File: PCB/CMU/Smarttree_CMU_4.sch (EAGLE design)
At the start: 43 parts, among them X2 057-006-0

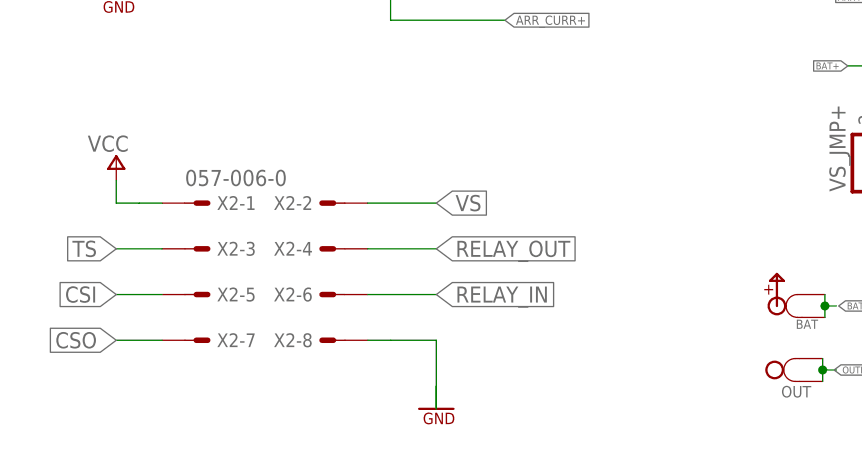
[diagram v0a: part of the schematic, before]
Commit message: new connector on cmu
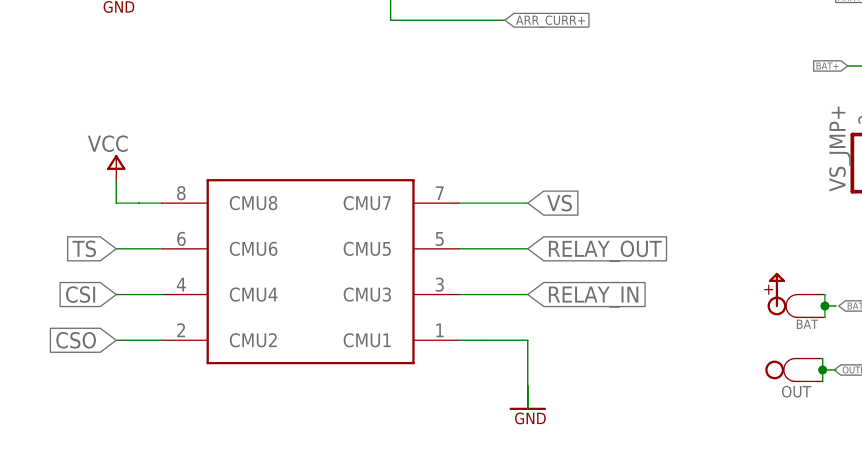
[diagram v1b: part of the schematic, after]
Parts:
- removed X2: 057-006-0, con-panduit:057-006-0
- added U$1: 8PINCONN, SmartTreeCan:8PINCONN
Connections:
- net CSI: now also U$1.CMU4; no longer X2-5.S
- net CSO: now also U$1.CMU2; no longer X2-7.S
- net GND: now also U$1.CMU1; no longer X2-8.S
- net RELAY_IN: now also U$1.CMU3; no longer X2-6.S
- net RELAY_OUT: now also U$1.CMU5; no longer X2-4.S
- net TS: now also U$1.CMU6; no longer X2-3.S
- net VCC: now also U$1.CMU8; no longer X2-1.S
- net VS: now also U$1.CMU7; no longer X2-2.S
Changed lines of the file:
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@@
 <layer number="54" name="bGND_GNDA" color="1" fill="9" visible="no" active="no"/>
 <layer number="56" name="wert" color="7" fill="1" visible="no" active="no"/>
+<layer number="57" name="tCAD" color="7" fill="1" visible="no" active="no"/>
+<layer number="59" name="tCarbon" color="7" fill="1" visible="no" active="no"/>
+<layer number="60" name="bCarbon" color="7" fill="1" visible="no" active="no"/>
 <layer number="90" name="Modules" color="5" fill="1" visible="yes" active="yes"/>
 <layer number="91" name="Nets" color="2" fill="1" visible="yes" active="yes"/>
@@
 <layer number="97" name="Info" color="7" fill="1" visible="no" active="yes"/>
 <layer number="98" name="Guide" color="6" fill="1" visible="no" active="yes"/>
+<layer number="99" name="SpiceOrder" color="7" fill="1" visible="yes" active="yes"/>
 <layer number="100" name="Muster" color="7" fill="1" visible="no" active="no"/>
 <layer number="101" name="Patch_Top" color="12" fill="4" visible="no" active="yes"/>
@@
 <layer number="111" name="LPC17xx" color="7" fill="1" visible="no" active="yes"/>
 <layer number="112" name="tSilk" color="7" fill="1" visible="no" active="yes"/>
+<layer number="113" name="IDFDebug" color="4" fill="1" visible="yes" active="yes"/>
 <layer number="116" name="Patch_BOT" color="9" fill="4" visible="no" active="yes"/>
+<layer number="118" name="Rect_Pads" color="7" fill="1" visible="yes" active="yes"/>
 <layer number="121" name="_tsilk" color="7" fill="1" visible="no" active="yes"/>
 <layer number="122" name="_bsilk" color="7" fill="1" visible="no" active="yes"/>
@@
 <layer number="127" name="_tValues" color="7" fill="1" visible="no" active="yes"/>
 <layer number="128" name="_bValues" color="7" fill="1" visible="no" active="yes"/>
+<layer number="129" name="Mask" color="7" fill="1" visible="yes" active="yes"/>
 <layer number="131" name="tAdjust" color="7" fill="1" visible="no" active="yes"/>
 <layer number="132" name="bAdjust" color="7" fill="1" visible="no" active="yes"/>
 <layer number="144" name="Drill_legend" color="7" fill="1" visible="no" active="yes"/>
+<layer number="150" name="Notes" color="7" fill="1" visible="yes" active="yes"/>
 <layer number="151" name="HeatSink" color="7" fill="1" visible="no" active="yes"/>
 <layer number="152" name="_bDocu" color="7" fill="1" visible="no" active="yes"/>
+<layer number="153" name="FabDoc1" color="7" fill="1" visible="yes" active="yes"/>
+<layer number="154" name="FabDoc2" color="7" fill="1" visible="yes" active="yes"/>
+<layer number="155" name="FabDoc3" color="7" fill="1" visible="yes" active="yes"/>
 <layer number="199" name="Contour" color="7" fill="1" visible="no" active="yes"/>
 <layer number="200" name="200bmp" color="1" fill="10" visible="no" active="yes"/>
@@
 <layer number="223" name="223bmp" color="24" fill="1" visible="no" active="no"/>
 <layer number="224" name="224bmp" color="25" fill="1" visible="no" active="no"/>
+<layer number="225" name="225bmp" color="7" fill="1" visible="yes" active="yes"/>
+<layer number="226" name="226bmp" color="7" fill="1" visible="yes" active="yes"/>
+<layer number="227" name="227bmp" color="7" fill="1" visible="yes" active="yes"/>
+<layer number="228" name="228bmp" color="7" fill="1" visible="yes" active="yes"/>
+<layer number="229" name="229bmp" color="7" fill="1" visible="yes" active="yes"/>
+<layer number="230" name="230bmp" color="7" fill="1" visible="yes" active="yes"/>
+<layer number="231" name="231bmp" color="7" fill="1" visible="yes" active="yes"/>
 <layer number="248" name="Housing" color="7" fill="1" visible="no" active="yes"/>
 <layer number="249" name="Edge" color="7" fill="1" visible="no" active="yes"/>
@@
 <layer number="251" name="SMDround" color="7" fill="1" visible="no" active="no"/>
 <layer number="254" name="cooling" color="7" fill="1" visible="no" active="yes"/>
+<layer number="255" name="routoute" color="7" fill="1" visible="yes" active="yes"/>
 </layers>
 <schematic xreflabel="%F%N/%S.%C%R" xrefpart="/%S.%C%R">
@@
 </variantdefs>
 <classes>
-<class number="0" name="default" width="0.4064" drill="0">
+<class number="0" name="default" width="0.254" drill="0">
 <clearance class="0" value="0.127"/>
 </class>
@@
 <part name="Q4" library="adafruit" deviceset="MOSFET-N" device="REFLOW"/>
 <part name="FRAME1" library="microbuilder" deviceset="FRAME_A4" device=""/>
-<part name="X2" library="con-panduit" deviceset="057-006-" device="0"/>
 <part name="SUPPLY15" library="eagle-book" deviceset="GND" device=""/>
 <part name="SUPPLY16" library="eagle-book" deviceset="VCC" device="" value="5V"/>
@@
 <part name="R14" library="adafruit" deviceset="R-US_" device="R0805" value="100"/>
 <part name="JP1" library="SparkFun" deviceset="M01" device="OFFSET" value="M01OFFSET"/>
+<part name="U$1" library="SmartTreeCan" deviceset="8PINCONN" device=""/>
 </parts>
 <sheets>
@@
 <instance part="Q4" gate="G$1" x="218.44" y="91.44" rot="MR0"/>
 <instance part="FRAME1" gate="G$1" x="0" y="0"/>
-<instance part="X2" gate="-1" x="48.26" y="33.02"/>
-<instance part="X2" gate="-8" x="60.96" y="17.78" rot="R180"/>
-<instance part="X2" gate="-3" x="48.26" y="27.94"/>
-<instance part="X2" gate="-6" x="60.96" y="22.86" rot="R180"/>
-<instance part="X2" gate="-5" x="48.26" y="22.86"/>
-<instance part="X2" gate="-4" x="60.96" y="27.94" rot="R180"/>
-<instance part="X2" gate="-7" x="48.26" y="17.78"/>
-<instance part="X2" gate="-2" x="60.96" y="33.02" rot="R180"/>
-<instance part="SUPPLY15" gate="GND" x="73.66" y="10.16"/>
+<instance part="SUPPLY15" gate="GND" x="83.82" y="10.16"/>
 <instance part="SUPPLY16" gate="1" x="38.1" y="38.1"/>
 <instance part="VS_JMP+" gate="G$1" x="124.968" y="36.83" rot="R90"/>
@@
 <attribute name="NAME" x="151.638" y="7.62" size="1.778" layer="95" rot="R90"/>
 </instance>
+<instance part="U$1" gate="G$1" x="58.42" y="25.4"/>
 </instances>
 <busses>
@@
 </segment>
 <segment>
-<pinref part="X2" gate="-8" pin="S"/>
-<wire x1="66.04" y1="17.78" x2="68.58" y2="17.78" width="0.1524" layer="91"/>
-<wire x1="68.58" y1="17.78" x2="73.66" y2="17.78" width="0.1524" layer="91"/>
+<wire x1="76.2" y1="17.78" x2="78.74" y2="17.78" width="0.1524" layer="91"/>
+<wire x1="78.74" y1="17.78" x2="83.82" y2="17.78" width="0.1524" layer="91"/>
 <pinref part="SUPPLY15" gate="GND" pin="GND"/>
-<wire x1="73.66" y1="17.78" x2="73.66" y2="10.16" width="0.1524" layer="91"/>
-<wire x1="73.66" y1="10.16" x2="73.66" y2="12.7" width="0.1524" layer="91"/>
+<wire x1="83.82" y1="17.78" x2="83.82" y2="10.16" width="0.1524" layer="91"/>
+<wire x1="83.82" y1="10.16" x2="83.82" y2="12.7" width="0.1524" layer="91"/>
+<pinref part="U$1" gate="G$1" pin="CMU1"/>
 </segment>
 <segment>
@@
 <net name="CSO" class="0">
 <segment>
-<pinref part="X2" gate="-7" pin="S"/>
 <wire x1="43.18" y1="17.78" x2="38.1" y2="17.78" width="0.1524" layer="91"/>
 <label x="38.1" y="17.78" size="1.778" layer="95" rot="R180" xref="yes"/>
+<pinref part="U$1" gate="G$1" pin="CMU2"/>
 </segment>
 <segment>
@@
 </segment>
 <segment>
-<pinref part="X2" gate="-1" pin="S"/>
 <wire x1="43.18" y1="33.02" x2="40.64" y2="33.02" width="0.1524" layer="91"/>
 <wire x1="40.64" y1="33.02" x2="38.1" y2="33.02" width="0.1524" layer="91"/>
 <pinref part="SUPPLY16" gate="1" pin="VCC"/>
 <wire x1="38.1" y1="33.02" x2="38.1" y2="35.56" width="0.1524" layer="91"/>
+<pinref part="U$1" gate="G$1" pin="CMU8"/>
 </segment>
 <segment>
@@
 </segment>
 <segment>
-<pinref part="X2" gate="-3" pin="S"/>
 <wire x1="43.18" y1="27.94" x2="38.1" y2="27.94" width="0.1524" layer="91"/>
 <label x="38.1" y="27.94" size="1.778" layer="95" rot="R180" xref="yes"/>
+<pinref part="U$1" gate="G$1" pin="CMU6"/>
 </segment>
 </net>
@@
 </segment>
 <segment>
-<pinref part="X2" gate="-2" pin="S"/>
-<wire x1="66.04" y1="33.02" x2="73.66" y2="33.02" width="0.1524" layer="91"/>
-<label x="73.66" y="33.02" size="1.778" layer="95" xref="yes"/>
+<wire x1="76.2" y1="33.02" x2="83.82" y2="33.02" width="0.1524" layer="91"/>
+<label x="83.82" y="33.02" size="1.778" layer="95" xref="yes"/>
+<pinref part="U$1" gate="G$1" pin="CMU7"/>
 </segment>
 </net>
@@
 <net name="RELAY_IN" class="0">
 <segment>
-<pinref part="X2" gate="-6" pin="S"/>
-<wire x1="66.04" y1="22.86" x2="73.66" y2="22.86" width="0.1524" layer="91"/>
-<label x="73.66" y="22.86" size="1.778" layer="95" xref="yes"/>
+<wire x1="76.2" y1="22.86" x2="83.82" y2="22.86" width="0.1524" layer="91"/>
+<label x="83.82" y="22.86" size="1.778" layer="95" xref="yes"/>
+<pinref part="U$1" gate="G$1" pin="CMU3"/>
 </segment>
 <segment>
@@
 <net name="RELAY_OUT" class="0">
 <segment>
-<pinref part="X2" gate="-4" pin="S"/>
-<wire x1="66.04" y1="27.94" x2="73.66" y2="27.94" width="0.1524" layer="91"/>
-<label x="73.66" y="27.94" size="1.778" layer="95" xref="yes"/>
+<wire x1="76.2" y1="27.94" x2="83.82" y2="27.94" width="0.1524" layer="91"/>
+<label x="83.82" y="27.94" size="1.778" layer="95" xref="yes"/>
+<pinref part="U$1" gate="G$1" pin="CMU5"/>
 </segment>
 <segment>
@@
 <net name="CSI" class="0">
 <segment>
-<pinref part="X2" gate="-5" pin="S"/>
 <wire x1="43.18" y1="22.86" x2="38.1" y2="22.86" width="0.1524" layer="91"/>
 <label x="38.1" y="22.86" size="1.778" layer="95" rot="R180" xref="yes"/>
-</segment>
-<segment>
+<pinref part="U$1" gate="G$1" pin="CMU4"/>
+</segment>
+<segment>

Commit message: revise resistor value for current sensor
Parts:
- R10: value 1k -> 10k
- R11: value 1k -> 330
- R12: value 10k -> 330
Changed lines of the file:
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@@
 <part name="C1" library="adafruit" deviceset="C-US" device="C0805" value="0.1uF"/>
 <part name="C2" library="adafruit" deviceset="C-US" device="C0805" value="0.1uF"/>
-<part name="R10" library="adafruit" deviceset="R-US_" device="R0805" value="1k"/>
+<part name="R10" library="adafruit" deviceset="R-US_" device="R0805" value="10k"/>
 <part name="SUPPLY17" library="eagle-book" deviceset="GND" device=""/>
 <part name="Z2" library="SparkFun" deviceset="DIODE-ZENER" device="-BZT52" value=""/>
 <part name="Z1" library="SparkFun" deviceset="DIODE-ZENER" device="-BZT52" value=""/>
-<part name="R11" library="adafruit" deviceset="R-US_" device="R0805" value="1k"/>
+<part name="R11" library="adafruit" deviceset="R-US_" device="R0805" value="330"/>
 <part name="SUPPLY18" library="eagle-book" deviceset="GND" device=""/>
-<part name="R12" library="adafruit" deviceset="R-US_" device="R0805" value="10k"/>
+<part name="R12" library="adafruit" deviceset="R-US_" device="R0805" value="330"/>
 <part name="SUPPLY19" library="eagle-book" deviceset="GND" device=""/>
 <part name="R13" library="adafruit" deviceset="R-US_" device="R0805" value="100"/>
